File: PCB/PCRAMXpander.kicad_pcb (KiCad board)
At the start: 2 copper layers, 22 parts, among them J1 Bus_ISA_16bit, U1 ATF16V8B-15PU, U2 SN74LVC16245ADGGR, U3 SN74LVC16244ADGGR, U4 SN74LVC16244ADGGR, U5 AS6C3216A-55TIN, U6 AS6C3216A-55TIN

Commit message: Routing has begun
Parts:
- removed RN1, RN2: 33 Ohm, Resistor_SMD:RESCAXE50P380X160X55-16N
- R1: footprint Resistor_SMD:RESCAV80P400X210X65-10N -> Project:RESCAV80P400X210X65-10N
- U1: footprint Connector:20P3_ATM -> Project:20P3_ATM
- U2: value SN74LVC16245ADGGR -> SN74LVCR16245ADGGR; footprint Package_TO_SOT_SMD:SOP50P810X120-48N -> Project:SOP50P810X120-48N
- U3, U4: footprint Package_SO:DGG0048A_N -> Project:DGG0048A_N
- U5, U6: footprint Package_TO_SOT_SMD:TSOP-I-48_12X20_ALL -> Project:TSOP-I-48_12X20_ALL
- VR1: footprint Transformer_SMD:LM1117IMPX-3.3_NOPB -> Package_SO:SOT230P700X180-4N
- moved C7 136.1 mm to (68.6, 135.6), turned to 90 degrees
- moved C8 113.3 mm to (82.5, 124.5), turned to 180 degrees
- moved C1 91.1 mm to (81.3, 86.4), turned to -90 degrees
- moved C4 91.1 mm to (116.8, 127.0)
- moved C3 89.6 mm to (141.1, 130.6), turned to 180 degrees
- moved VR1 88.9 mm to (78.7, 133.3)
- moved JP1 82.5 mm to (69.6, 99.1)
- moved C2 79.5 mm to (130.8, 114.3), turned to 180 degrees
- moved U4 71.5 mm to (108.1, 133.6)
- moved C5 68.5 mm to (104.1, 91.4)
- moved U3 66.3 mm to (133.5, 133.3)
- moved JP2 61.5 mm to (94.9, 94.5)
- moved JP3 54.1 mm to (177.8, 121.9)
- moved R1 53.8 mm to (96.3, 105.0)
- moved U1 53.0 mm to (73.7, 91.4)
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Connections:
- J1 pad 10: unconnected-(J1-GND-Pad10) -> GND
- J1 pad 29: unconnected-(J1-VCC-Pad29) -> +5V
- J1 pad 63: unconnected-(J1-~{MEMCS16}-Pad63) -> MEMCS16
- U2 pad 26: Net-(U2-2A8) -> Net-(J1-D15)
- U2 pad 27: Net-(U2-2A7) -> Net-(J1-D14)
- U2 pad 29: Net-(U2-2A6) -> Net-(J1-D13)
- U2 pad 30: Net-(U2-2A5) -> Net-(J1-D12)
- U2 pad 32: Net-(U2-2A4) -> Net-(J1-D11)
- U2 pad 33: Net-(U2-2A3) -> Net-(J1-D10)
- U2 pad 35: Net-(U2-2A2) -> Net-(J1-D9)
- U2 pad 36: Net-(U2-2A1) -> Net-(J1-D8)
- U2 pad 37: Net-(U2-1A8) -> Net-(J1-DB7)
- U2 pad 38: Net-(U2-1A7) -> Net-(J1-DB6)
- U2 pad 40: Net-(U2-1A6) -> Net-(J1-DB5)
- U2 pad 41: Net-(U2-1A5) -> Net-(J1-DB4)
- U2 pad 43: Net-(U2-1A4) -> Net-(J1-DB3)
- U2 pad 44: Net-(U2-1A3) -> Net-(J1-DB2)
- U2 pad 46: Net-(U2-1A2) -> Net-(J1-DB1)
- U2 pad 47: Net-(U2-1A1) -> Net-(J1-DB0)
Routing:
- net +5V: track 0.00 -> 154.7 mm, vias 0 -> 1
- net +3.3V: track 0.00 -> 110.3 mm, vias 0 -> 6
- net Net-(JP3-A): track 0.00 -> 103.7 mm, vias 0 -> 1
- net BA01: track 0.00 -> 30.4 mm
- net BA14: track 0.00 -> 28.5 mm, vias 0 -> 2
- net BA16: track 0.00 -> 28.3 mm
- net BA15: track 0.00 -> 28.2 mm, vias 0 -> 2
- net BA02: track 0.00 -> 27.7 mm
- net BA13: track 0.00 -> 26.2 mm, vias 0 -> 2
- net BA12: track 0.00 -> 25.1 mm, vias 0 -> 2
- net BA03: track 0.00 -> 24.8 mm
- net Net-(J1-NOWS): track 0.00 -> 24.1 mm
- net BA11: track 0.00 -> 23.0 mm, vias 0 -> 2
- net BA04: track 0.00 -> 22.1 mm
- net BA10: track 0.00 -> 21.3 mm, vias 0 -> 2
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- added copper zone on B.Cu, net GND
- added copper zone on F.Cu, net GND
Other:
- board outline added: 134.6 x 97.8 mm

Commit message: Playing with routing a bit more
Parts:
- added R2: 10k, Resistor_SMD:R_0805_2012Metric_Pad1.20x1.40mm_HandSolder, F.Cu at (72.6, 117.9)
- added R3: 10 kOhm, Project:RESCAV80P400X210X65-10N, F.Cu at (121.9, 74.3)
- R1: value 10 kOhm -> 10k; footprint Project:RESCAV80P400X210X65-10N -> Resistor_SMD:R_0805_2012Metric_Pad1.20x1.40mm_HandSolder
- moved U5 34.3 mm to (142.2, 64.5)
- moved C5 31.9 mm to (127.6, 69.8), turned to 180 degrees
- moved R1 31.7 mm to (67.3, 117.9), turned to 90 degrees
- moved JP2 28.6 mm to (70.4, 109.2), turned to 180 degrees
- moved C2 11.7 mm to (119.8, 110.5)
- moved U2 8.71 mm to (116.3, 103.9)
- moved U4 6.93 mm to (113.1, 128.7)
- moved C6 5.72 mm to (128.9, 92.7), turned to 180 degrees
- moved U1 5.08 mm to (78.7, 91.4)
- moved C4 4.93 mm to (121.7, 126.0), turned to 180 degrees
- moved U3 4.64 mm to (133.7, 128.7), turned to 180 degrees
- moved C3 4.47 mm to (142.2, 126.2)
- moved C1 4.32 mm to (85.6, 86.4), turned to 0 degrees
- moved JP1 1.48 mm to (70.4, 97.8)
- moved C8 1.27 mm to (81.8, 123.4)
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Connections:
- R1 pad 1: +3.3V -> +5V
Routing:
- net +5V: track 154.7 -> 253.7 mm, vias 1 -> 2
- net LA21: track 0.00 -> 86.7 mm, vias 0 -> 5
- net LA20: track 0.00 -> 85.3 mm, vias 0 -> 3
- net LA23: track 0.00 -> 72.1 mm, vias 0 -> 2
- net LA22: track 0.00 -> 68.5 mm, vias 0 -> 2
- net A18: track 0.00 -> 66.1 mm
- net Net-(J1-D15): track 0.00 -> 65.4 mm
- net A20: track 0.00 -> 65.2 mm
- net A19: track 0.00 -> 63.2 mm
- net Net-(J1-D14): track 0.00 -> 63.1 mm
- net A17: track 0.00 -> 61.7 mm
- net Net-(J1-D13): track 0.00 -> 61.4 mm
- net Net-(J1-D12): track 0.00 -> 59.4 mm
- net CS_HI: track 0.00 -> 59.2 mm, vias 0 -> 3
- net Net-(J1-D11): track 0.00 -> 57.6 mm
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
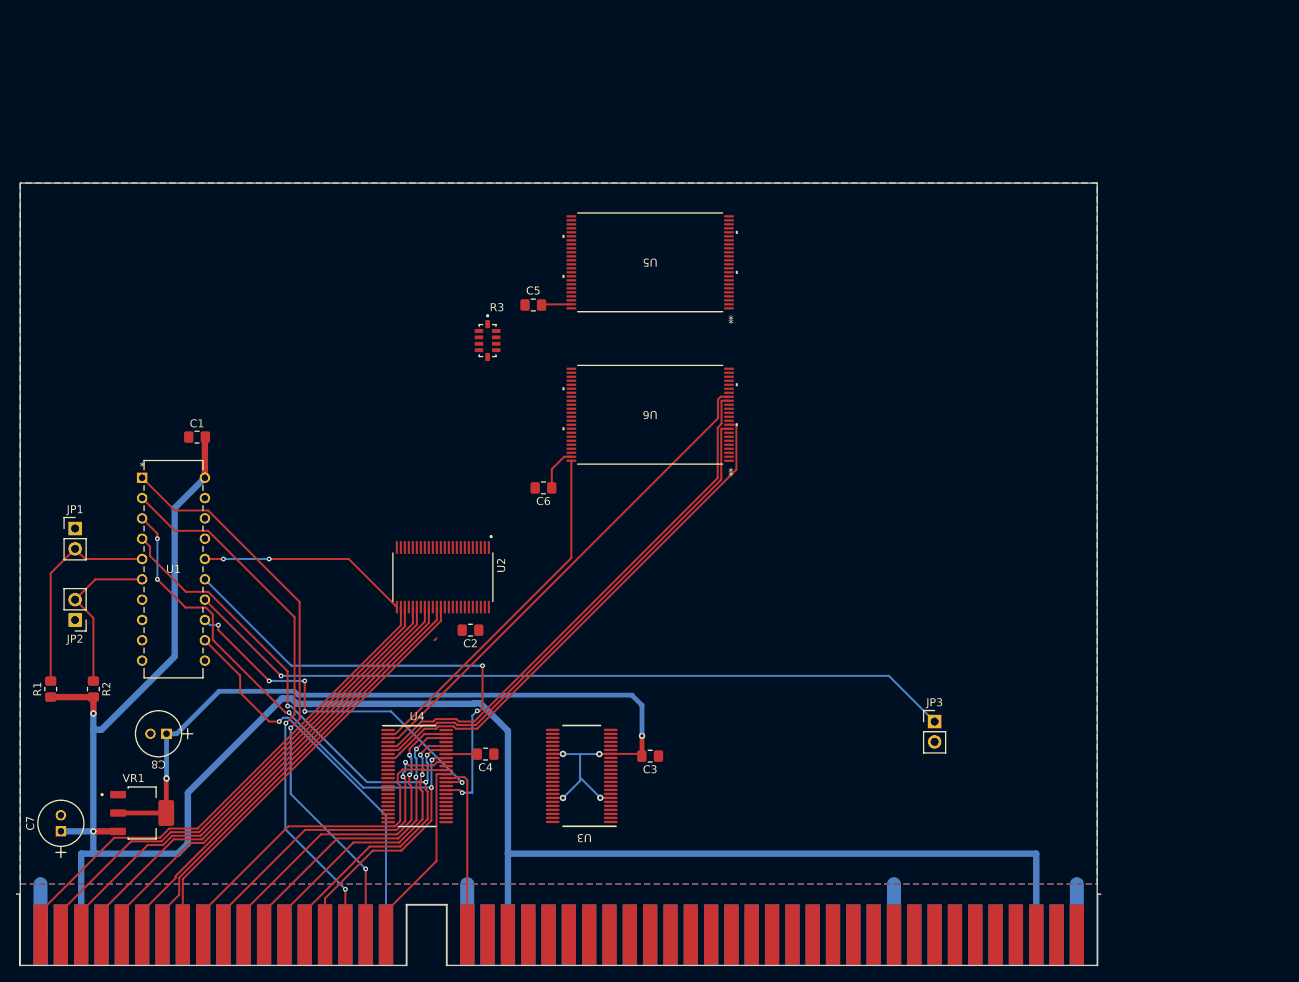
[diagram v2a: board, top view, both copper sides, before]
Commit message: Power routing only
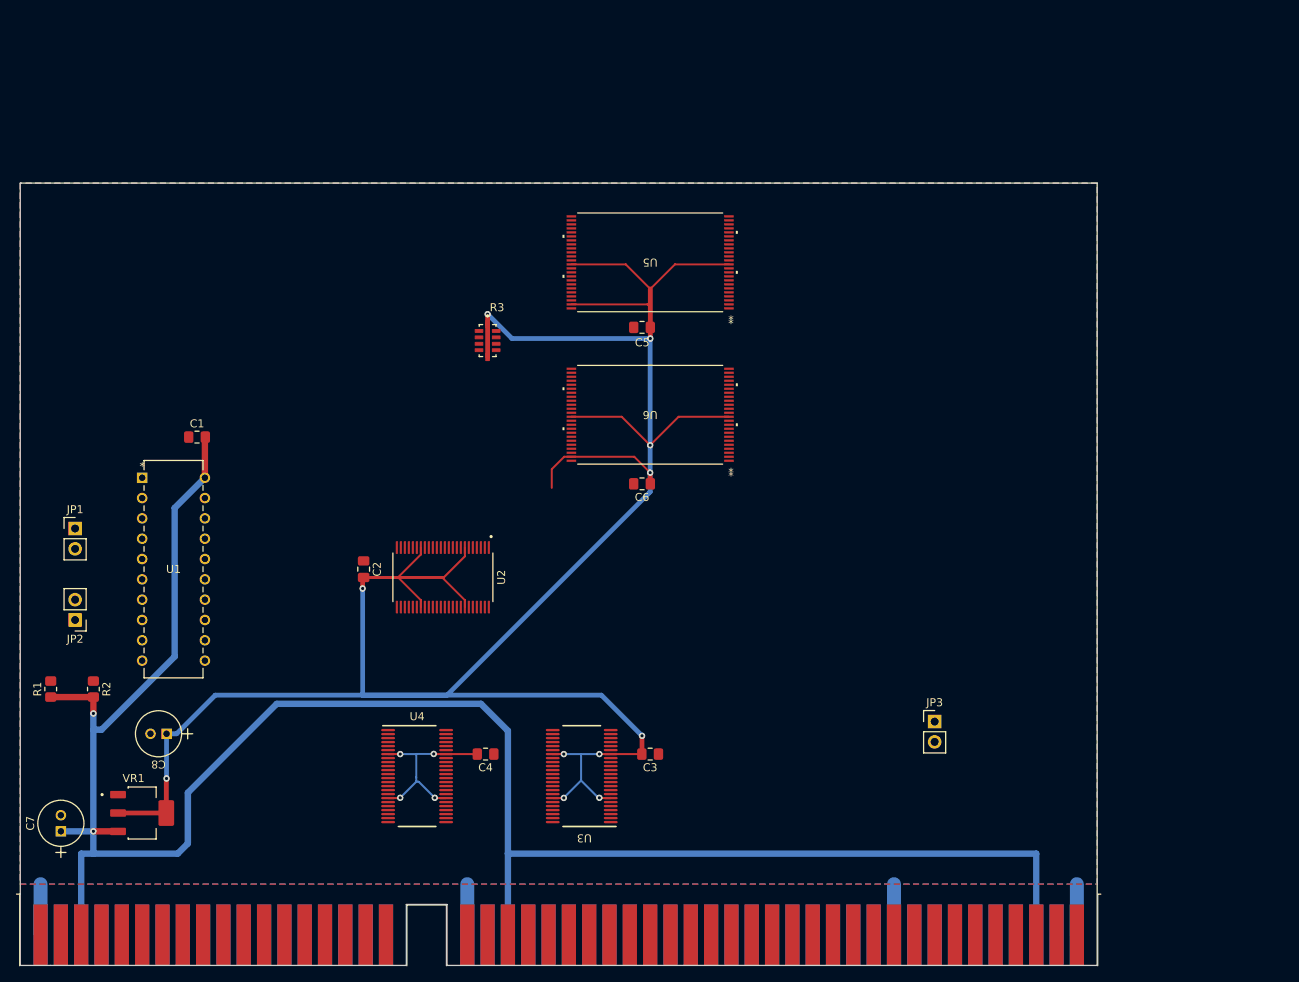
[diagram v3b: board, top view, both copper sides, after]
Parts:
- moved C2 15.4 mm to (106.4, 102.9), turned to -90 degrees
- moved C5 13.9 mm to (141.2, 72.6)
- moved C6 12.3 mm to (141.2, 92.2)
- moved C3 0.25 mm to (142.2, 126.0)
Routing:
- net +3.3V: track 121.6 -> 363.8 mm, vias 6 -> 15
- net Net-(JP3-A): track 97.5 -> 0.00 mm, vias 1 -> 0
- net LA21: track 86.7 -> 0.00 mm, vias 5 -> 0
- net LA20: track 85.3 -> 0.00 mm, vias 3 -> 0
- net LA23: track 72.1 -> 0.00 mm, vias 2 -> 0
- net LA22: track 68.5 -> 0.00 mm, vias 2 -> 0
- net A18: track 66.1 -> 0.00 mm
- net Net-(J1-D15): track 65.4 -> 0.00 mm
- net A20: track 65.2 -> 0.00 mm
- net A19: track 63.2 -> 0.00 mm
- net Net-(J1-D14): track 63.1 -> 0.00 mm
- net A17: track 61.7 -> 0.00 mm
- net Net-(J1-D13): track 61.4 -> 0.00 mm
- net Net-(J1-D12): track 59.4 -> 0.00 mm
- net CS_HI: track 59.2 -> 0.00 mm, vias 3 -> 0
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
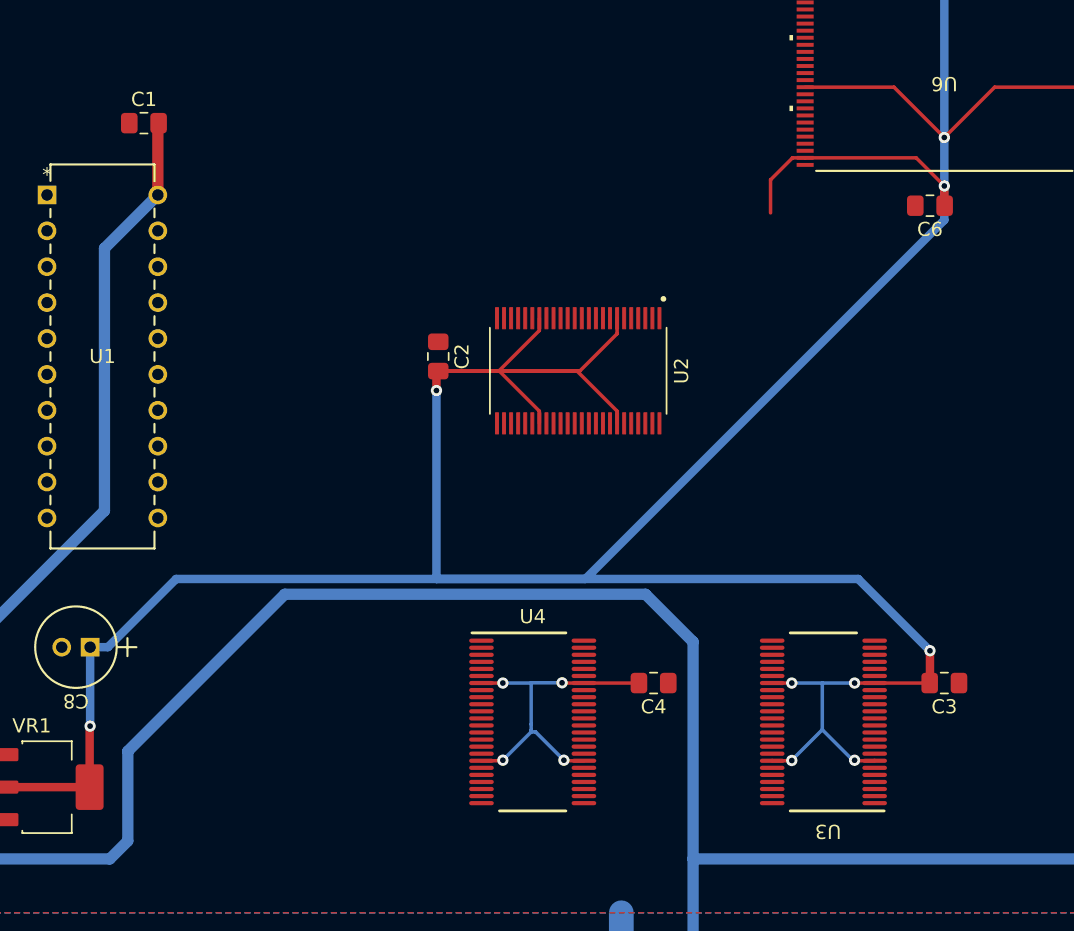
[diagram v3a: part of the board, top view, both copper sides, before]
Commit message: Potentially improved chip orientation
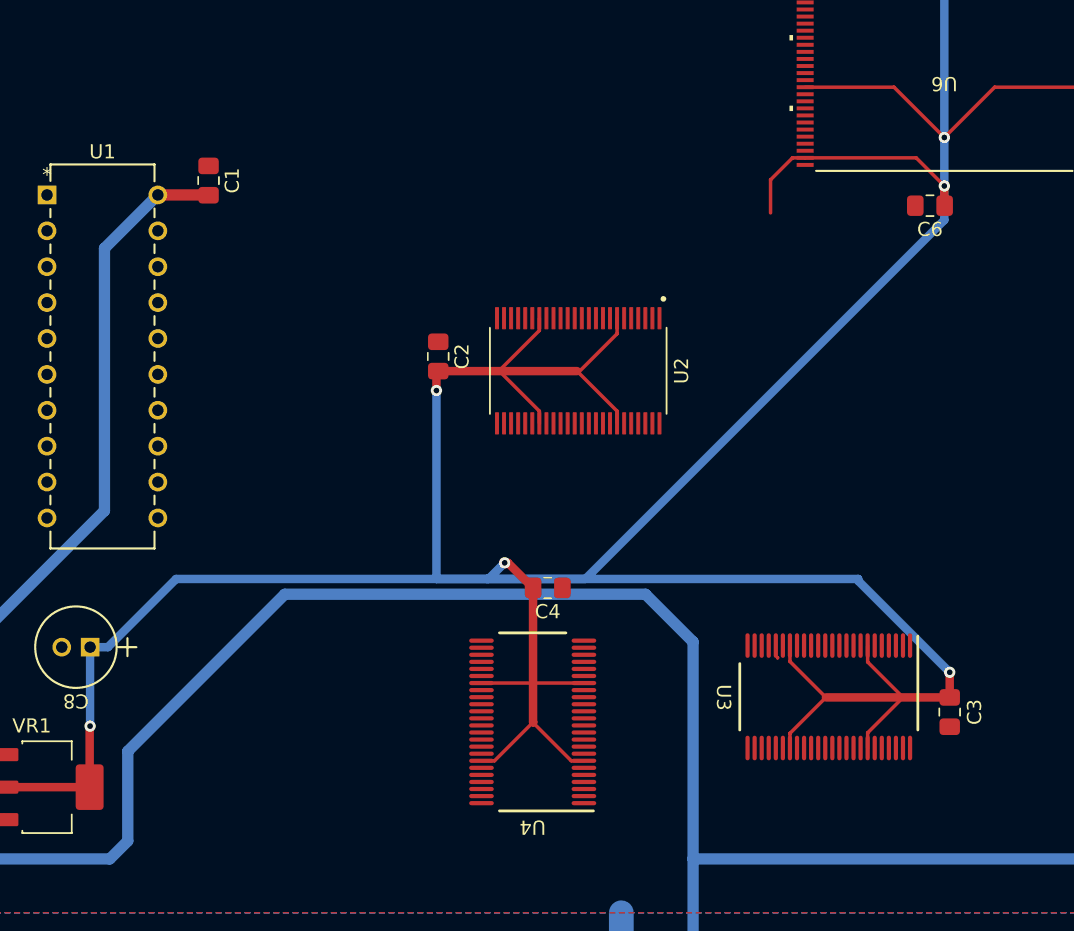
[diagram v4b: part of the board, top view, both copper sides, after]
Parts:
- moved C4 10.1 mm to (114.2, 119.3)
- moved C1 6.12 mm to (90.2, 90.4), turned to -90 degrees
- moved C3 2.09 mm to (142.6, 128.0), turned to 90 degrees
- moved U3 1.82 mm to (134.1, 127.0), turned to -90 degrees
- turned U4 to 180 degrees
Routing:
- net +3.3V: track 363.8 -> 357.0 mm, vias 15 -> 8
- net +5V: track 253.1 -> 251.6 mm

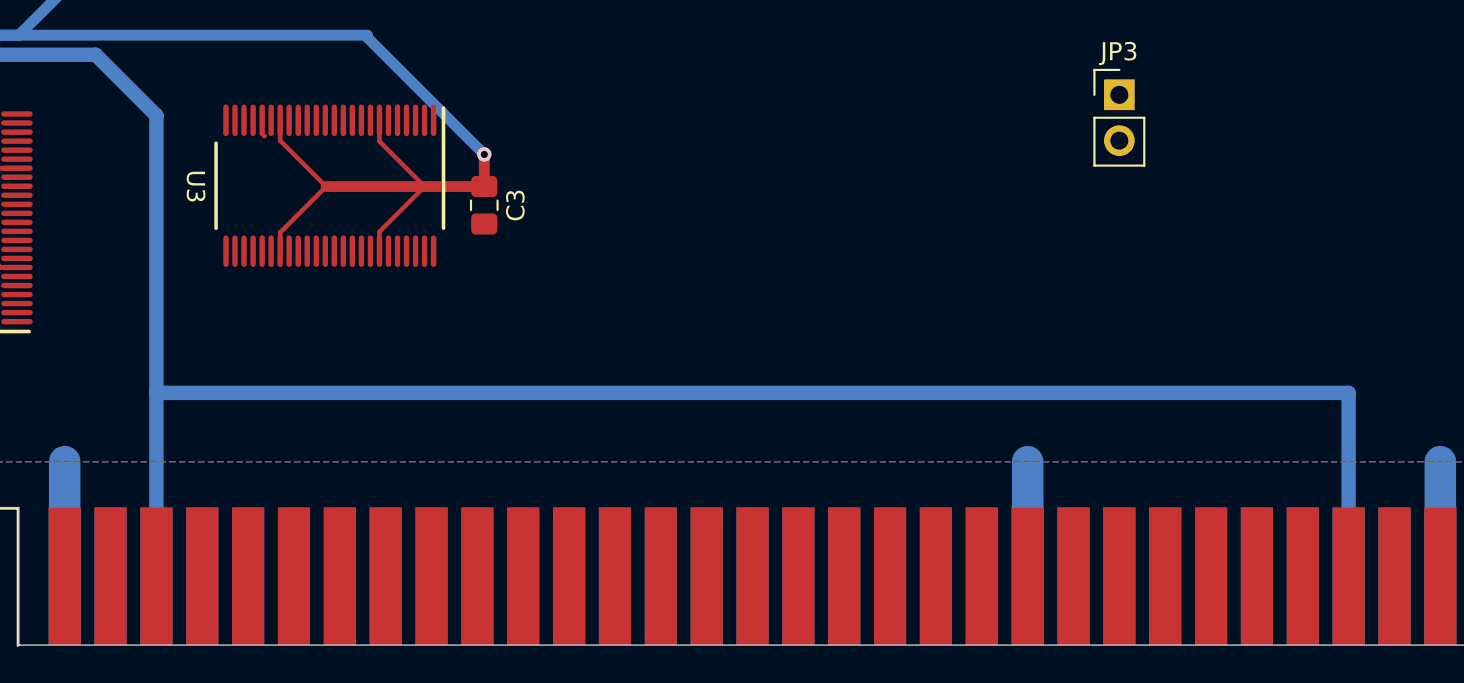
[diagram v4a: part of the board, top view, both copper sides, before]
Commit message: manual routing of U3 right side
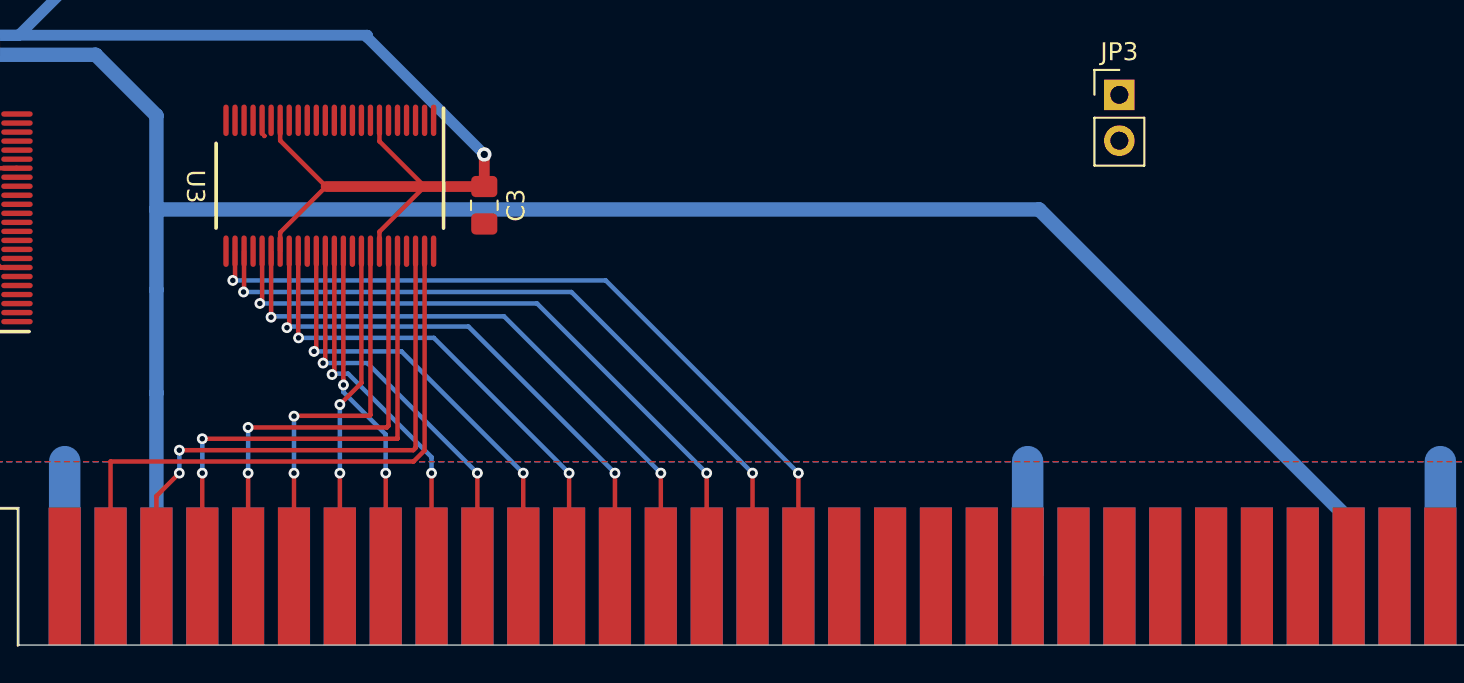
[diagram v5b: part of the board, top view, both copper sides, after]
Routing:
- net BA16: track 0.00 -> 43.1 mm, vias 0 -> 2
- net BA15: track 0.00 -> 40.3 mm, vias 0 -> 2
- net BA14: track 0.00 -> 37.3 mm, vias 0 -> 2
- net BA01: track 0.00 -> 35.1 mm
- net BA13: track 0.00 -> 34.6 mm, vias 0 -> 2
- net BA12: track 0.00 -> 31.6 mm, vias 0 -> 2
- net BA02: track 0.00 -> 31.5 mm, vias 0 -> 2
- net BA03: track 0.00 -> 28.8 mm, vias 0 -> 2
- net BA11: track 0.00 -> 28.6 mm, vias 0 -> 2
- net BA04: track 0.00 -> 25.7 mm, vias 0 -> 2
- net BA10: track 0.00 -> 25.7 mm, vias 0 -> 2
- net BA09: track 0.00 -> 23.0 mm, vias 0 -> 2
- net BA05: track 0.00 -> 22.2 mm, vias 0 -> 2
- net BA08: track 0.00 -> 20.9 mm, vias 0 -> 2
- net BA07: track 0.00 -> 19.0 mm, vias 0 -> 2
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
